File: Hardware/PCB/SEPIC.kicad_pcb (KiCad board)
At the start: 2 copper layers, 37.5 x 28.5 mm, 33 parts, among them Q1 IRFR024PBF, Q2 AO3401A, U1 LM3478MA

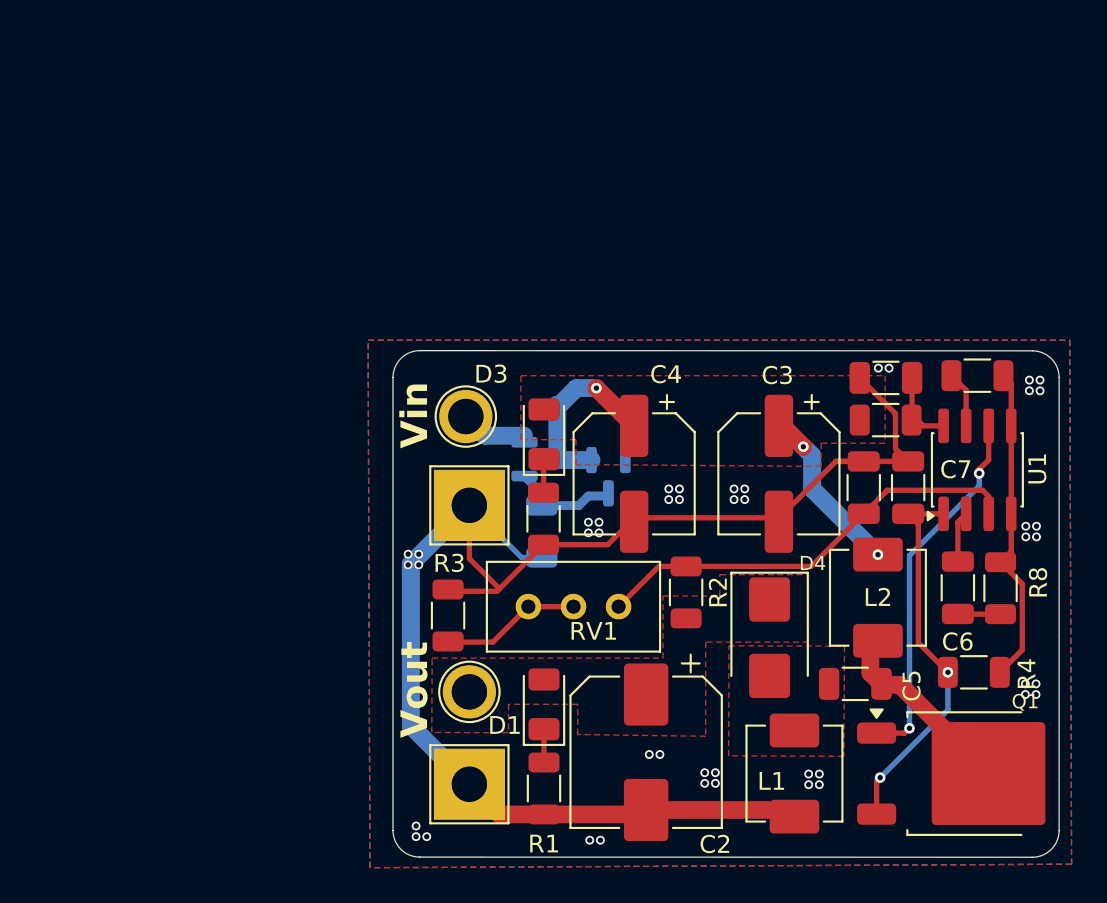
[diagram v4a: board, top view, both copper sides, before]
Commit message: Update PCB footprints, layout and schematic positions
Replace/standardize several footprints (LM3478 -> SOIC-8, DPAK MOSFET removed, Vishay IHLP inductor footprint added), adjust silkscreen references and pad positions, retune pad nets, add vias, routing segments and copper zones, and tidy fp_line/fp_poly outlines. Synchronize schematic symbol coordinates to match new PCB placement. Also update SEPIC.kicad_pro used_designators (added D5,Z1). These edits reorganize the SEPIC board layout and BOM footprints for manufacturability and correct net/pin assignments.
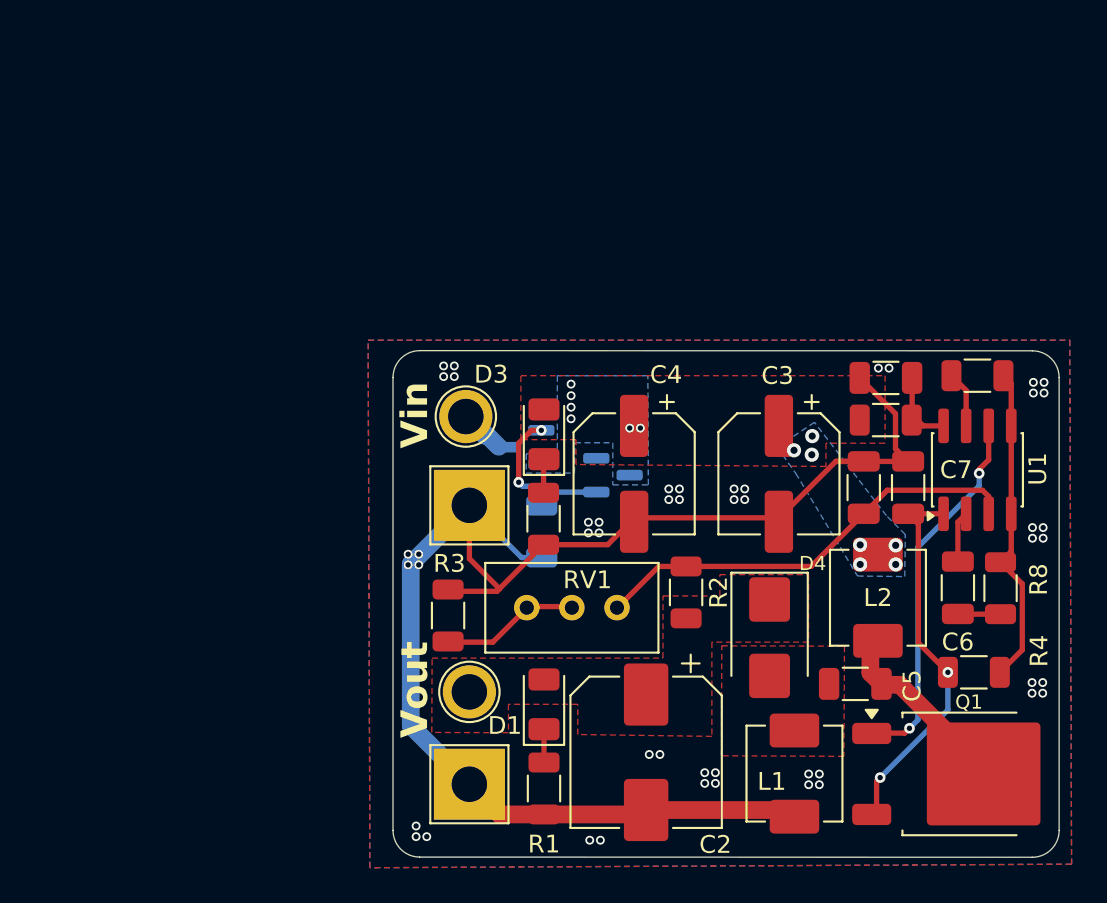
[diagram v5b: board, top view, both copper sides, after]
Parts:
- moved G*** 4.32 mm to (107.9, 65.2)
- moved Q2 1.15 mm to (98.8, 56.6), turned to 180 degrees
- moved G*** 0.41 mm to (124.8, 65.2)
- moved Q1 0.28 mm to (123.4, 75.0)
- moved D2 0.27 mm to (103.8, 58.2), turned to 0 degrees
- moved RV1 0.11 mm to (104.0, 65.7)
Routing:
- net /Vbus: track 20.4 -> 0.05 mm, vias 3 -> 13
- net Net-(D2-A): track 6.10 -> 9.16 mm, vias 0 -> 2
- net Vin: track 3.72 -> 2.55 mm
- net GND: vias 45 -> 49
- added copper zone on B.Cu, net /Vbus

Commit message: update and backup
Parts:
- C6: value 10n -> 100n
- C8: value 100p -> 100n
- R2: value 100k -> 15k
- R3: value 5k -> 1k
- R4: value 0.05 -> 1m
- R7: value 40k -> 120k
- R8: value 150 -> 1
- RV1: value 100k -> 10k
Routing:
- net /Isen: track 21.5 -> 22.3 mm
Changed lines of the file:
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@@
 			)
 		)
-		(property "Value" "10n"
+		(property "Value" "100n"
 			(at 0 1.85 90)
 			(layer "F.Fab")
@@
 			)
 		)
-		(property "Value" "100p"
+		(property "Value" "100n"
 			(at 0 1.85 0)
 			(layer "F.Fab")
@@
 			)
 		)
-		(property "Value" "5k"
+		(property "Value" "1k"
 			(at 0 1.83 90)
 			(layer "F.Fab")
@@
 			)
 		)
-		(property "Value" "100k"
+		(property "Value" "15k"
 			(at 0 1.83 90)
 			(layer "F.Fab")
@@
 			)
 		)
-		(property "Value" "40k"
+		(property "Value" "120k"
 			(at 0 1.83 0)
 			(layer "F.Fab")
@@
 			)
 		)
-		(property "Value" "150"
+		(property "Value" "1"
 			(at 0 1.83 90)
 			(layer "F.Fab")
@@
 			)
 		)
-		(property "Value" "0.05"
+		(property "Value" "1m"
 			(at 0 1.83 0)
 			(layer "F.Fab")
@@
 			)
 		)
-		(property "Value" "100k"
+		(property "Value" "10k"
 			(at -2.54 3.67 0)
 			(layer "F.Fab")
@@
 		(start 120.4 60.375)
 		(end 122.395 60.375)
-		(width 0.3)
+		(width 1)
 		(layer "F.Cu")
 		(net "/Isen")
 	)
 	(segment
-		(start 120.975 60.95)
-		(end 120.975 67.6375)
-		(width 0.3)
+		(start 118.625 75.425)
+		(end 118.625 77.28)
+		(width 1)
 		(layer "F.Cu")
 		(net "/Isen")
 	)
 	(segment
-		(start 120.975 67.6375)
-		(end 122.6375 69.3)
+		(start 118.975 75.075)
+		(end 118.625 75.425)
 		(width 0.3)
 		(layer "F.Cu")
@@
 	)
 	(segment
-		(start 120.4 60.375)
-		(end 120.975 60.95)
-		(width 0.3)
+		(start 120.975 60.95)
+		(end 120.975 67.6375)
+		(width 1)
 		(layer "F.Cu")
 		(net "/Isen")
 	)
 	(segment
-		(start 118.625 75.425)
-		(end 118.825 75.225)
-		(width 0.3)
+		(start 120.975 67.6375)
+		(end 122.6375 69.3)
+		(width 1)
 		(layer "F.Cu")
 		(net "/Isen")
 	)
 	(segment
-		(start 118.625 77.28)
-		(end 118.625 75.425)
-		(width 0.3)
+		(start 120.4 60.375)
+		(end 120.975 60.95)
+		(width 1)
 		(layer "F.Cu")
 		(net "/Isen")
@@
 	(via
 		(at 122.6375 69.3)
-		(size 0.6)
-		(drill 0.3)
+		(size 0.8)
+		(drill 0.4)
 		(layers "F.Cu" "B.Cu")
 		(net "/Isen")
 	)
 	(via
-		(at 118.825 75.225)
-		(size 0.6)
-		(drill 0.3)
+		(at 118.975 75.075)
+		(size 0.8)
+		(drill 0.4)
 		(layers "F.Cu" "B.Cu")
 		(net "/Isen")
 	)
 	(segment
-		(start 118.825 75.225)
+		(start 122.6375 72.7875)
 		(end 122.6375 71.4125)
-		(width 0.3)
+		(width 1)
 		(layer "B.Cu")
 		(net "/Isen")
@@
 		(start 122.6375 71.4125)
 		(end 122.6375 69.3)
-		(width 0.3)
+		(width 1)
+		(layer "B.Cu")
+		(net "/Isen")
+	)
+	(segment
+		(start 120.35 75.075)
+		(end 122.6375 72.7875)
+		(width 1)
+		(layer "B.Cu")
+		(net "/Isen")
+	)
+	(segment
+		(start 118.975 75.075)
+		(end 120.35 75.075)
+		(width 1)
 		(layer "B.Cu")
 		(net "/Isen")

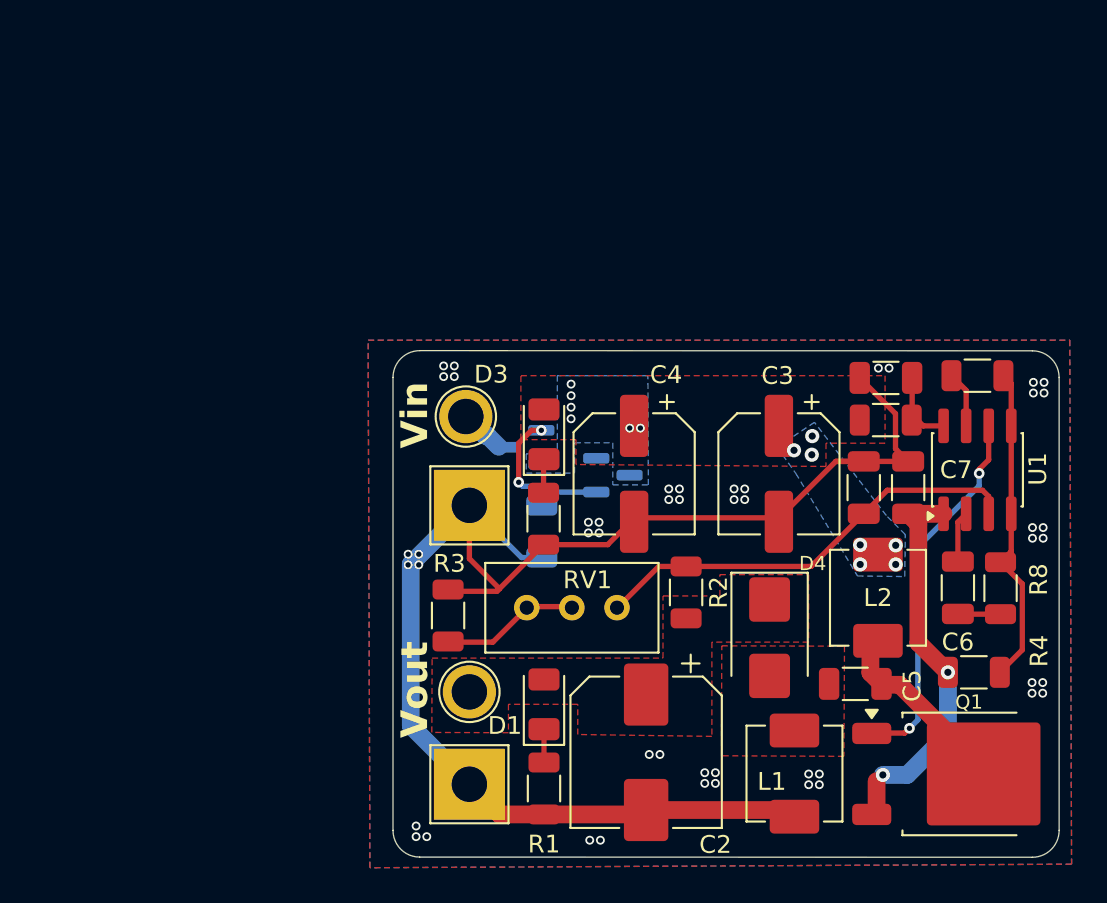
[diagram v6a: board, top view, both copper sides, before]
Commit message: Calculation value update
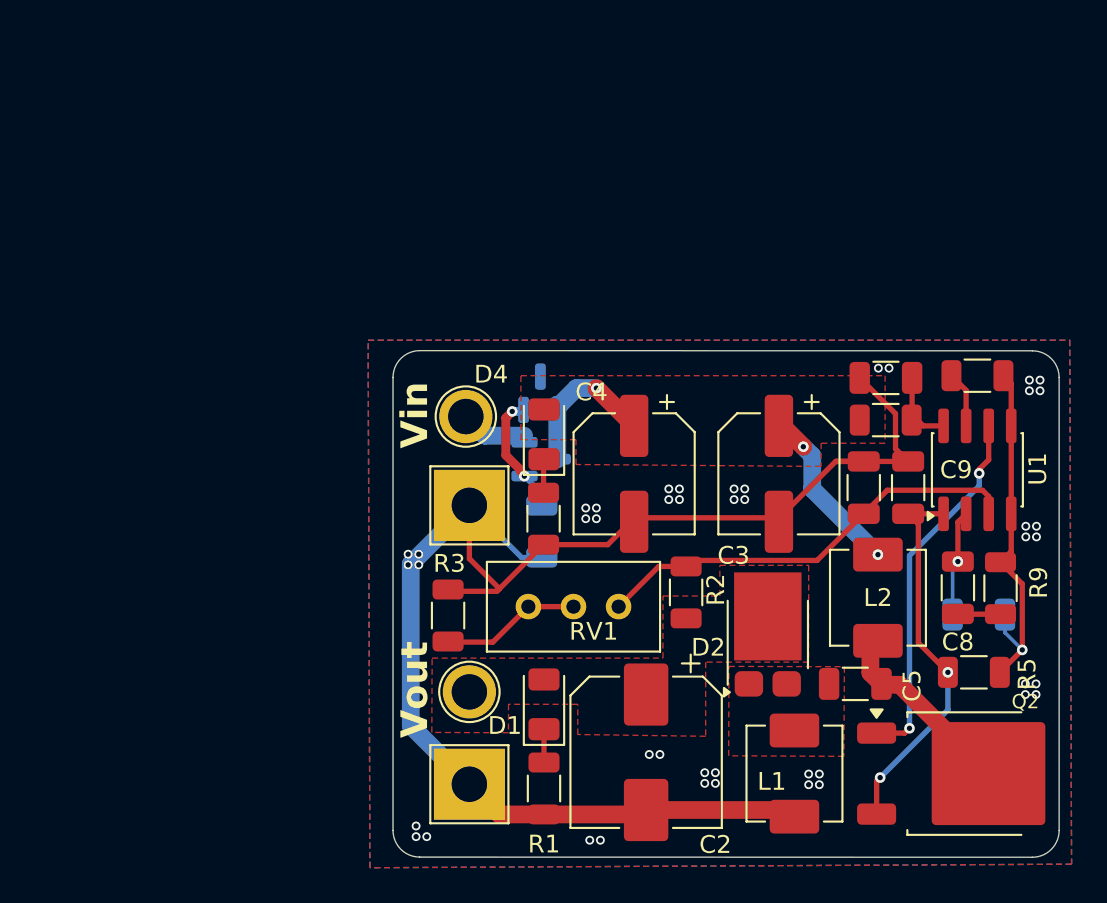
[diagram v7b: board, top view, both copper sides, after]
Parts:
- removed the D4 at (112.6, 67.3)
- removed the Q1 at (123.4, 75.0)
- added C7: 4,7n, Capacitor_SMD:C_1206_3216Metric, B.Cu at (124.4, 66.0)
- added D3: BZX84-A10,215, Package_TO_SOT_SMD:SOT-23, B.Cu at (99.7, 53.6)
- added Q2: IRFR024PBF, IRFR024:IRFR024PBF, F.Cu at (123.7, 75.0)
- C2: value 100u -> 560u
- C5: value 1u -> 10u
- C8: renamed from C6; value 100n -> 220n
- D2: value BZX84-A10,215 -> PMEG045T030EPDZ; footprint BZX84:SOT-23 -> Package_TO_SOT_SMD:Nexperia_CFP15_SOT-1289; moved to F.Cu
- R1: value 1k -> 2.2k
- R5: renamed from R4; value 1m -> 20m
- R8: renamed from R7; value 120k -> 20k
- R9: renamed from R8; value 1 -> 2.5k
- moved D2 12.5 mm to (112.5, 67.2), turned to 90 degrees
- moved G*** 8.15 mm to (124.5, 73.3)
- moved G*** 4.32 mm to (112.1, 64.0)
- moved Q1 1.15 mm to (99.7, 57.3), turned to 0 degrees
- moved RV1 0.11 mm to (104.1, 65.6)
- renumbered C8 to C6, C7 to C9, D3 to D4, Q2 to Q1, R9 to R4, R5 to R7
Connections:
- C5 pad 1: Net-(D4-A) -> Net-(D2-A_1)
- D2 pad 1: /Vbus -> Net-(D2-A_1)
- D2 pad 2: Net-(D2-A) -> Net-(D2-A_1)
- L1 pad 2: Net-(D4-A) -> Net-(D2-A_1)
- Q1 pad 1: Net-(D2-A) -> Net-(D3-A)
- R4 pad 1: Net-(D2-A) -> Net-(D3-A)
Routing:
- net /Vbus: track 0.05 -> 18.5 mm, vias 13 -> 3
- net Net-(D2-A): track 9.16 -> 0.00 mm, vias 2 -> 0
- net Net-(D3-A): track 0.00 -> 6.93 mm, vias 0 -> 2
- net Net-(U1-COMP): track 2.88 -> 5.99 mm, vias 0 -> 1
- net GND: track 103.5 -> 105.8 mm, vias 49 -> 46
- net Vin: track 2.55 -> 3.72 mm
- net /Isen: track 22.3 -> 21.5 mm
- added copper zone on F.Cu, net Net-(D2-A_1)
- removed copper zone on B.Cu, net /Vbus
- removed copper zone on F.Cu, net Net-(D4-A)

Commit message: EOD PCB commit
End Of Development update, after compiling the data in a spreadsheet, I replaced the diode and the MOSFET, and also copied the calculated values for the passive components.
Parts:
- removed the D3 at (99.7, 53.6)
- added Z1: BZX84-A10,215, Package_TO_SOT_SMD:SOT-23, B.Cu at (100.1, 53.6)
- C7: moved to F.Cu
- Q2: value IRFR024PBF -> AO4262E; footprint IRFR024:IRFR024PBF -> Package_SO:SOIC-8_3.9x4.9mm_P1.27mm
- moved G*** 6.91 mm to (124.1, 66.4)
- moved C7 2.28 mm to (124.2, 68.3)
- moved R7 1.78 mm to (124.2, 71.1)
- moved Q2 0.86 mm to (123.3, 75.8)
- renumbered D4 to D3, R6 to R5, R7 to R6, R5 to R7
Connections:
- C5 pad 2: Net-(Q2-D) -> Net-(Q2-S_1)
- L2 pad 2: Net-(Q2-D) -> Net-(Q2-S_1)
- Q2 pad 1: Net-(Q2-D) -> Net-(Q2-S_1)
- Q2 pad 2: /DR -> Net-(Q2-S_1)
- Q2 pad 3: /Isen -> Net-(Q2-S_1)
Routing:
- net /Isen: track 21.5 -> 0.00 mm, vias 2 -> 0
- net Net-(Q2-D): track 12.2 -> 0.00 mm
- net /DR: track 20.8 -> 24.2 mm
- net Net-(U1-COMP): track 5.99 -> 9.13 mm, vias 1 -> 2
- net GND: track 105.8 -> 105.2 mm, vias 46 -> 51
- net Net-(Q2-S_1): track 0.00 -> 0.60 mm
- added copper zone on F.Cu, net /Isen
- added copper zone on F.Cu, net Net-(Q2-S_1)
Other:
- board text added: "Vin : 3-12 V Vout : 3-20 V Max power: 30 W"
- board text removed: "Vin : 3-20 V Vout : 3-20 V Max I : 3 A const."
